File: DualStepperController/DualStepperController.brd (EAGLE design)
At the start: 69.8 x 57.1 mm, 14 parts

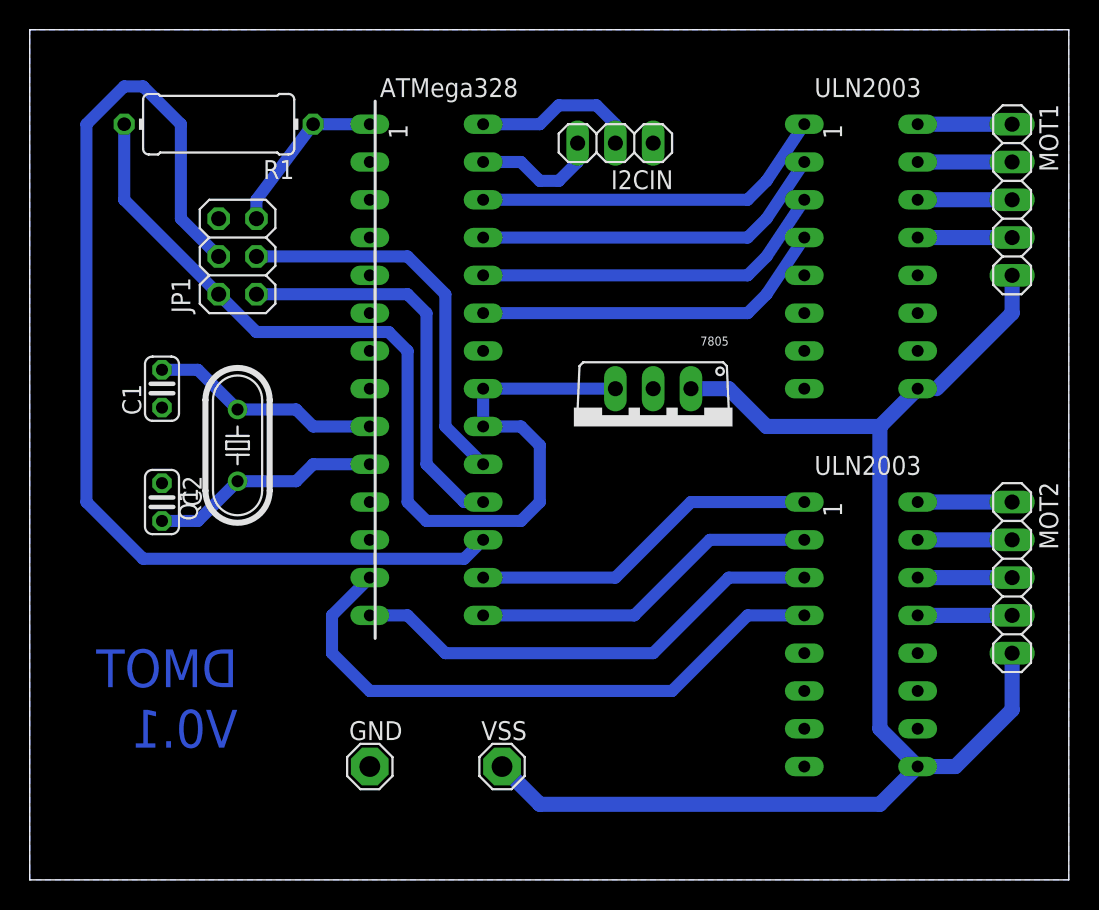
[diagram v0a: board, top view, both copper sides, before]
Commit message: Add mounting holes.
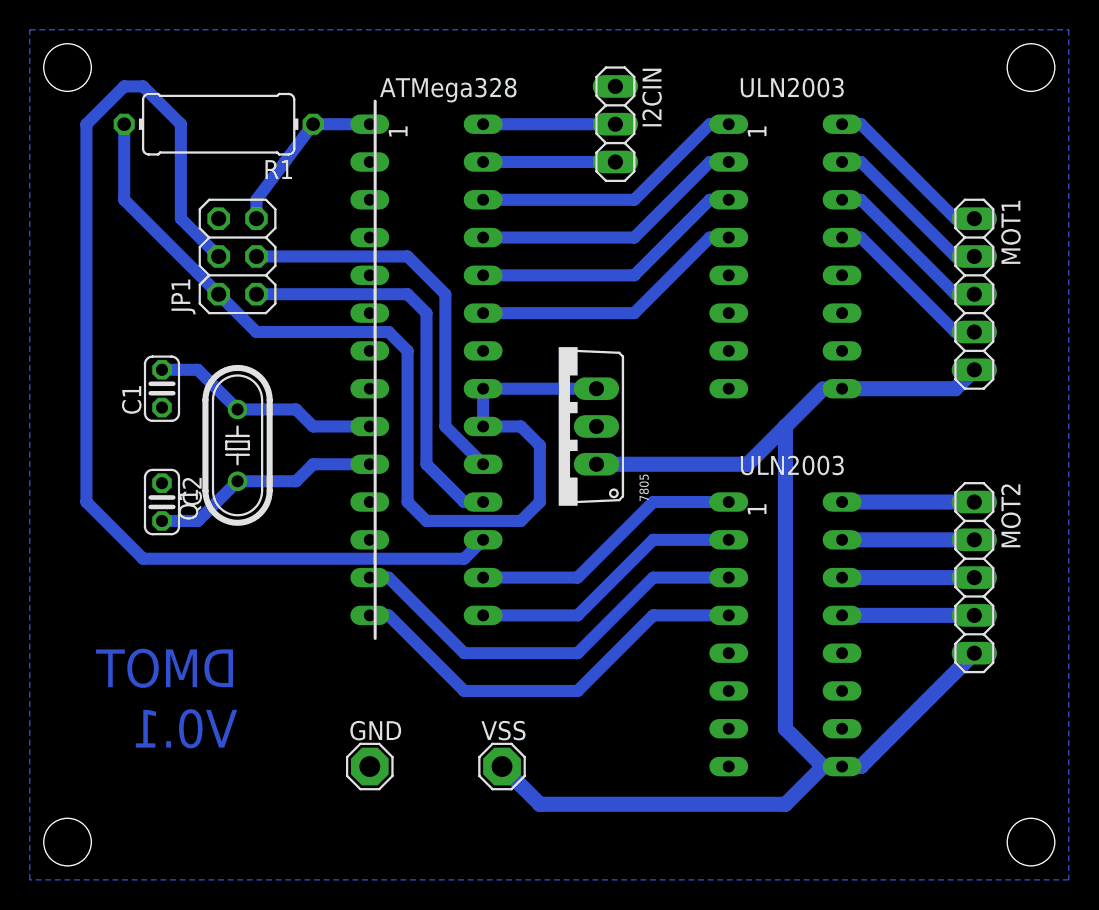
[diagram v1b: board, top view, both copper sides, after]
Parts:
- moved MOT1 6.84 mm to (63.5, 39.4)
- moved U$4 6.35 mm to (35.6, 30.5), turned to 90 degrees
- moved U$2 5.08 mm to (50.8, 41.9)
- moved U$3 5.08 mm to (50.8, 16.5)
- moved MOT2 2.54 mm to (63.5, 20.3)
- moved I2CIN 1.27 mm to (39.4, 50.8), turned to 270 degrees
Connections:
- net N$24: now also U$3.4; no longer U$3.3
- net N$25: now also U$3.3; no longer U$3.4
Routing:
- net N$25: track 41.0 -> 28.3 mm
- net N$21: track 24.2 -> 18.6 mm
- net N$20: track 24.2 -> 18.6 mm
- net N$19: track 24.2 -> 18.6 mm
- net N$18: track 24.2 -> 18.6 mm
- net N$4: track 6.35 -> 11.5 mm
- net N$3: track 6.35 -> 11.5 mm
- net N$2: track 6.35 -> 11.5 mm
- net N$1: track 6.35 -> 11.5 mm
- net VSS: track 94.0 -> 89.0 mm
- net N$23: track 23.7 -> 18.6 mm
- net N$22: track 23.7 -> 18.6 mm
- net N$24: track 32.4 -> 28.3 mm
- net N$9: track 6.35 -> 8.89 mm
- net N$8: track 6.35 -> 8.89 mm
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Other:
- board outline removed

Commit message: Add serial header to Dual Stepper Controller. Add a new project for a ESP breakout board.
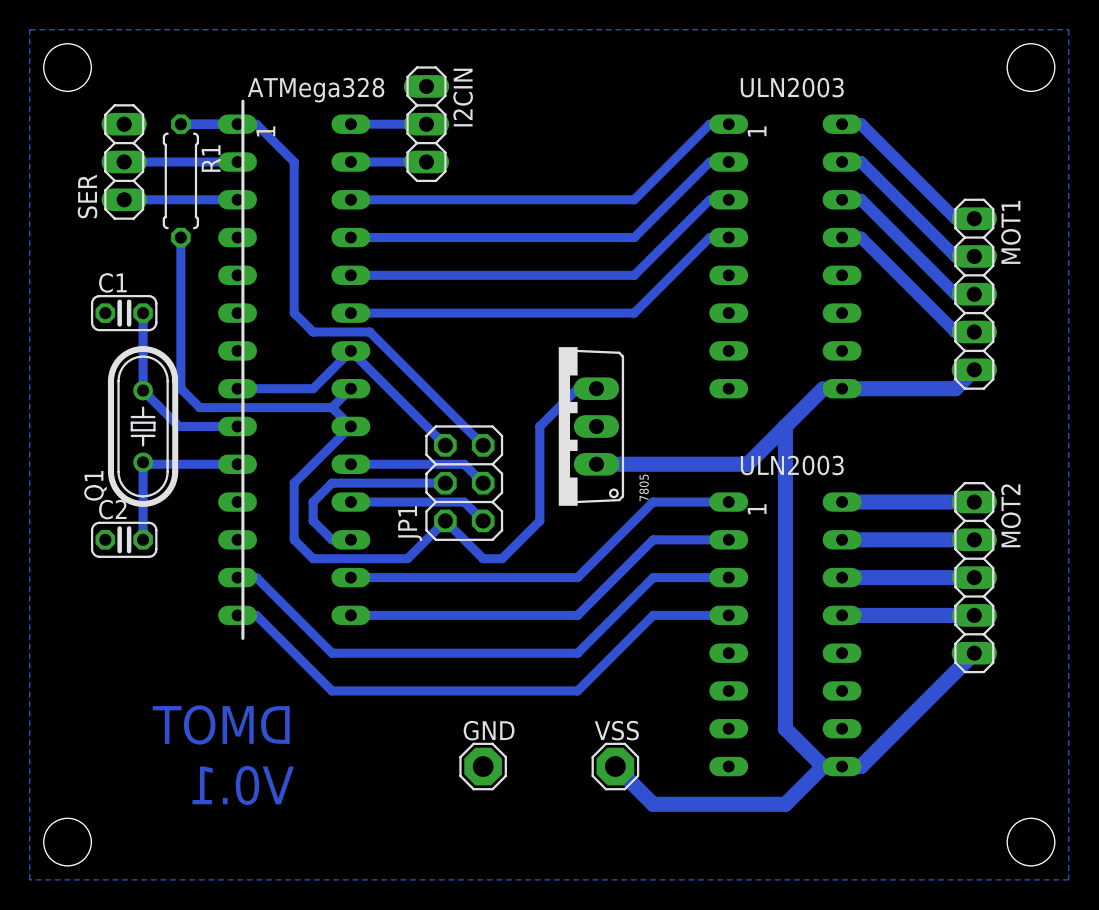
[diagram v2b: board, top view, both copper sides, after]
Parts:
- added SER: (no value), pinhead:1X03
- R1: device rcl:0411/12 -> rcl:0207/7
- moved JP1 21.6 mm to (29.2, 26.7)
- moved I2CIN 12.7 mm to (26.7, 50.8)
- moved U$1 8.89 mm to (17.8, 34.3)
- moved GND 7.62 mm to (30.5, 7.62)
- moved VSS 7.62 mm to (39.4, 7.62)
- moved Q1 6.48 mm to (7.62, 30.5)
- moved C1 5.68 mm to (6.35, 38.1), turned to 0 degrees
- moved R1 4.58 mm to (10.2, 47.0), turned to 270 degrees
- moved C2 3.59 mm to (6.35, 22.9), turned to 0 degrees
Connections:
- new net N$13: SER.1, U$1.3
- new net N$26: SER.2, U$1.2
- net GND: now also SER.3
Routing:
- net N$17: track 72.6 -> 13.8 mm
- net N$14: track 11.4 -> 39.0 mm
- net GND: track 0.00 -> 17.7 mm
- net N$15: track 27.0 -> 9.42 mm
- net N$16: track 26.2 -> 9.42 mm
- net N$23: track 18.6 -> 27.5 mm
- net N$22: track 18.6 -> 27.5 mm
- net N$21: track 18.6 -> 27.5 mm
- net N$20: track 18.6 -> 27.5 mm
- net N$19: track 18.6 -> 27.5 mm
- net N$18: track 18.6 -> 27.5 mm
- net N$25: track 28.3 -> 37.2 mm
- net N$24: track 28.3 -> 37.2 mm
- net N$26: track 0.00 -> 7.62 mm
- net N$13: track 0.00 -> 7.62 mm
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
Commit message: Move board outline to document layer.
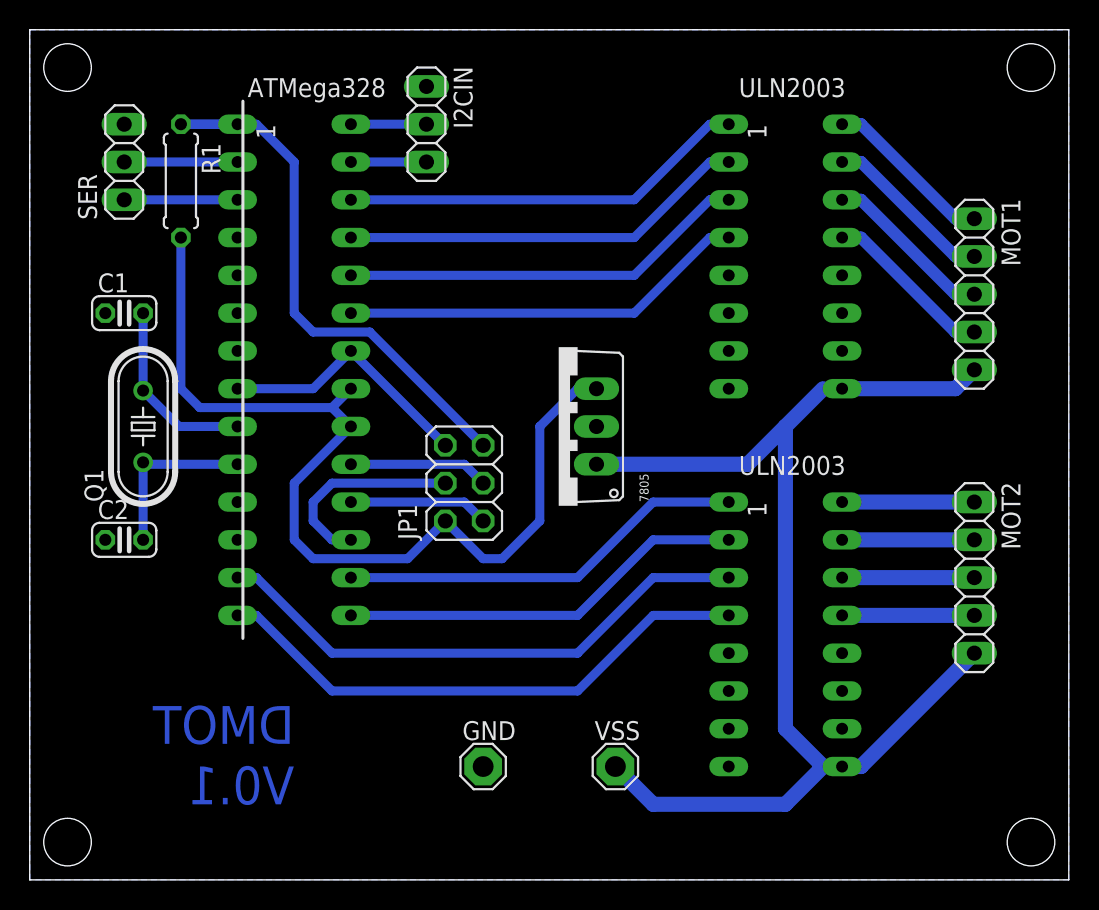
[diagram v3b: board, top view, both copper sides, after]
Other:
- board outline added: 69.8 x 57.1 mm
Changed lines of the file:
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@@
 <grid distance="0.05" unitdist="inch" unit="inch" style="lines" multiple="1" display="no" altdistance="0.025" altunitdist="inch" altunit="inch"/>
 <layers>
-<layer number="1" name="Top" color="4" fill="1" visible="no" active="yes"/>
+<layer number="1" name="Top" color="4" fill="1" visible="yes" active="yes"/>
 <layer number="16" name="Bottom" color="1" fill="1" visible="yes" active="yes"/>
 <layer number="17" name="Pads" color="2" fill="1" visible="yes" active="yes"/>
@@
 <layer number="23" name="tOrigins" color="15" fill="1" visible="yes" active="yes"/>
 <layer number="24" name="bOrigins" color="15" fill="1" visible="yes" active="yes"/>
-<layer number="25" name="tNames" color="7" fill="1" visible="yes" active="yes"/>
+<layer number="25" name="tNames" color="7" fill="1" visible="no" active="yes"/>
 <layer number="26" name="bNames" color="7" fill="1" visible="no" active="yes"/>
-<layer number="27" name="tValues" color="7" fill="1" visible="yes" active="yes"/>
+<layer number="27" name="tValues" color="7" fill="1" visible="no" active="yes"/>
 <layer number="28" name="bValues" color="7" fill="1" visible="no" active="yes"/>
 <layer number="29" name="tStop" color="7" fill="3" visible="no" active="yes"/>
@@
 <layer number="48" name="Document" color="7" fill="1" visible="yes" active="yes"/>
 <layer number="49" name="Reference" color="7" fill="1" visible="yes" active="yes"/>
-<layer number="51" name="tDocu" color="7" fill="1" visible="yes" active="yes"/>
+<layer number="51" name="tDocu" color="7" fill="1" visible="no" active="yes"/>
 <layer number="52" name="bDocu" color="7" fill="1" visible="no" active="yes"/>
 <layer number="90" name="Modules" color="5" fill="1" visible="no" active="no"/>
@@
 <text x="17.78" y="5.08" size="2.54" layer="16" font="vector" ratio="15" distance="60" rot="MR0">DMOT
 V0.1</text>
-<wire x1="0" y1="57.15" x2="69.85" y2="57.15" width="0" layer="24"/>
-<wire x1="69.85" y1="57.15" x2="69.85" y2="0" width="0" layer="24"/>
-<wire x1="69.85" y1="0" x2="0" y2="0" width="0" layer="24"/>
-<wire x1="0" y1="0" x2="0" y2="57.15" width="0" layer="24"/>
+<wire x1="0" y1="57.15" x2="69.85" y2="57.15" width="0" layer="20"/>
+<wire x1="69.85" y1="57.15" x2="69.85" y2="0" width="0" layer="20"/>
+<wire x1="69.85" y1="0" x2="0" y2="0" width="0" layer="20"/>
+<wire x1="0" y1="0" x2="0" y2="57.15" width="0" layer="20"/>
 <hole x="2.54" y="54.61" drill="3.2"/>
 <hole x="67.31" y="54.61" drill="3.2"/>
@@
 <contactref element="JP1" pad="6"/>
 <contactref element="U$4" pad="GND"/>
-<polygon width="0.8128" layer="16" isolate="0.4064">
+<polygon width="0.6096" layer="16" isolate="0.4064">
 <vertex x="0" y="57.15"/>
 <vertex x="69.85" y="57.15"/>
@@
 <wire x1="19.05" y1="33.02" x2="21.59" y2="35.56" width="0.6096" layer="16"/>
 <contactref element="SER" pad="3"/>
-<wire x1="27.94" y1="29.21" x2="38.1" y2="30.48" width="0" layer="19" extent="1-1"/>
 </signal>
 <signal name="VSS">
